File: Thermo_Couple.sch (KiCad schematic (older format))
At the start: 0 parts

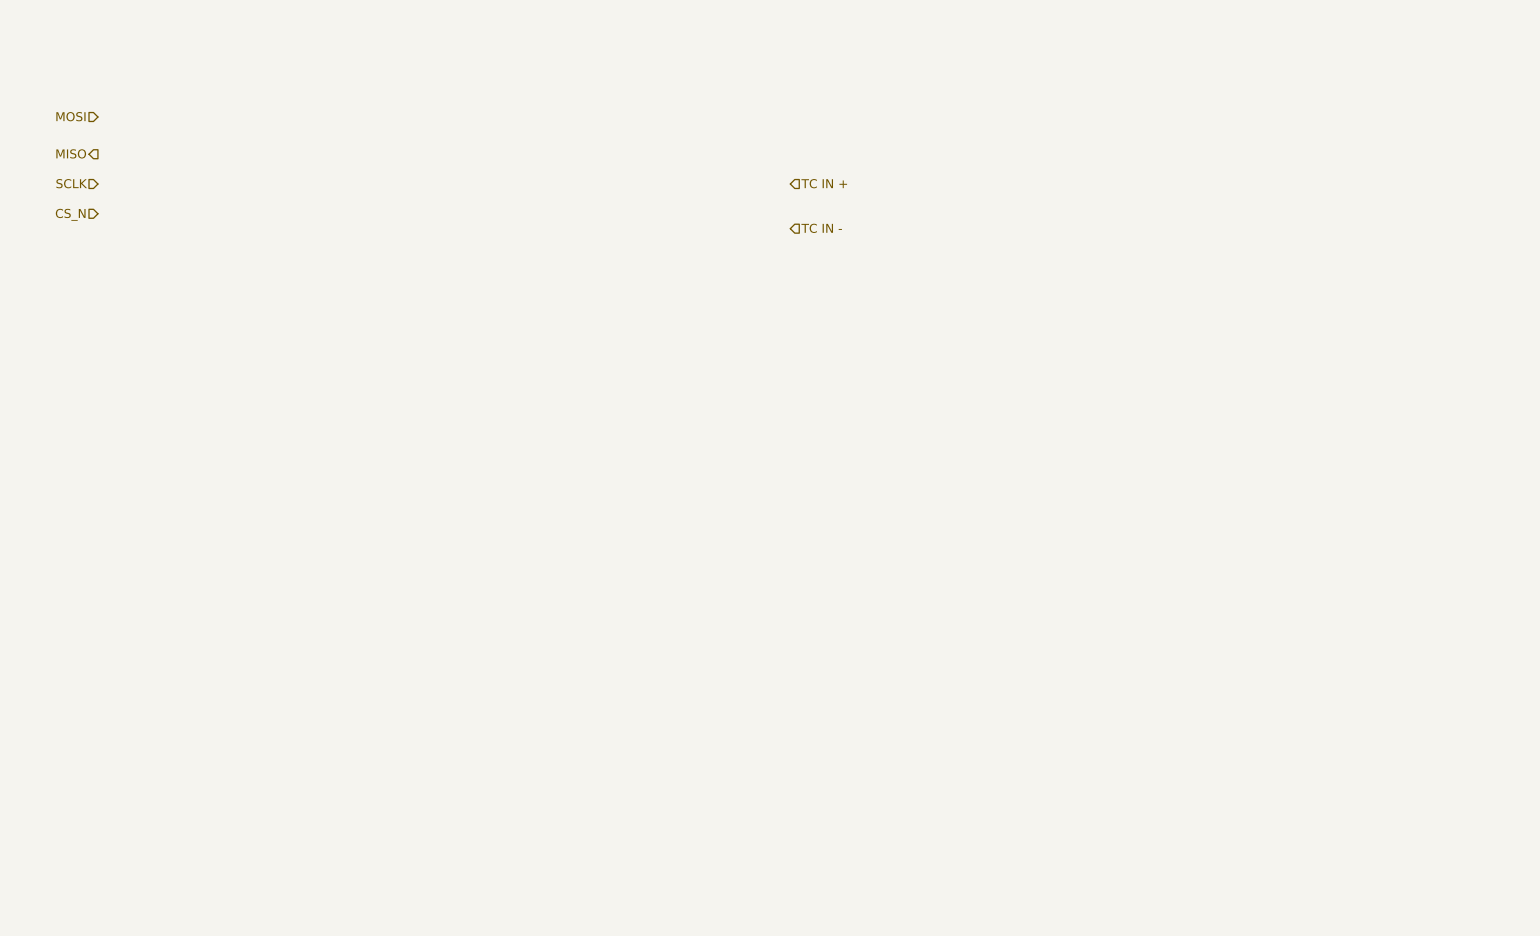
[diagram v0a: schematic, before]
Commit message: Wire Up general Thermocouple
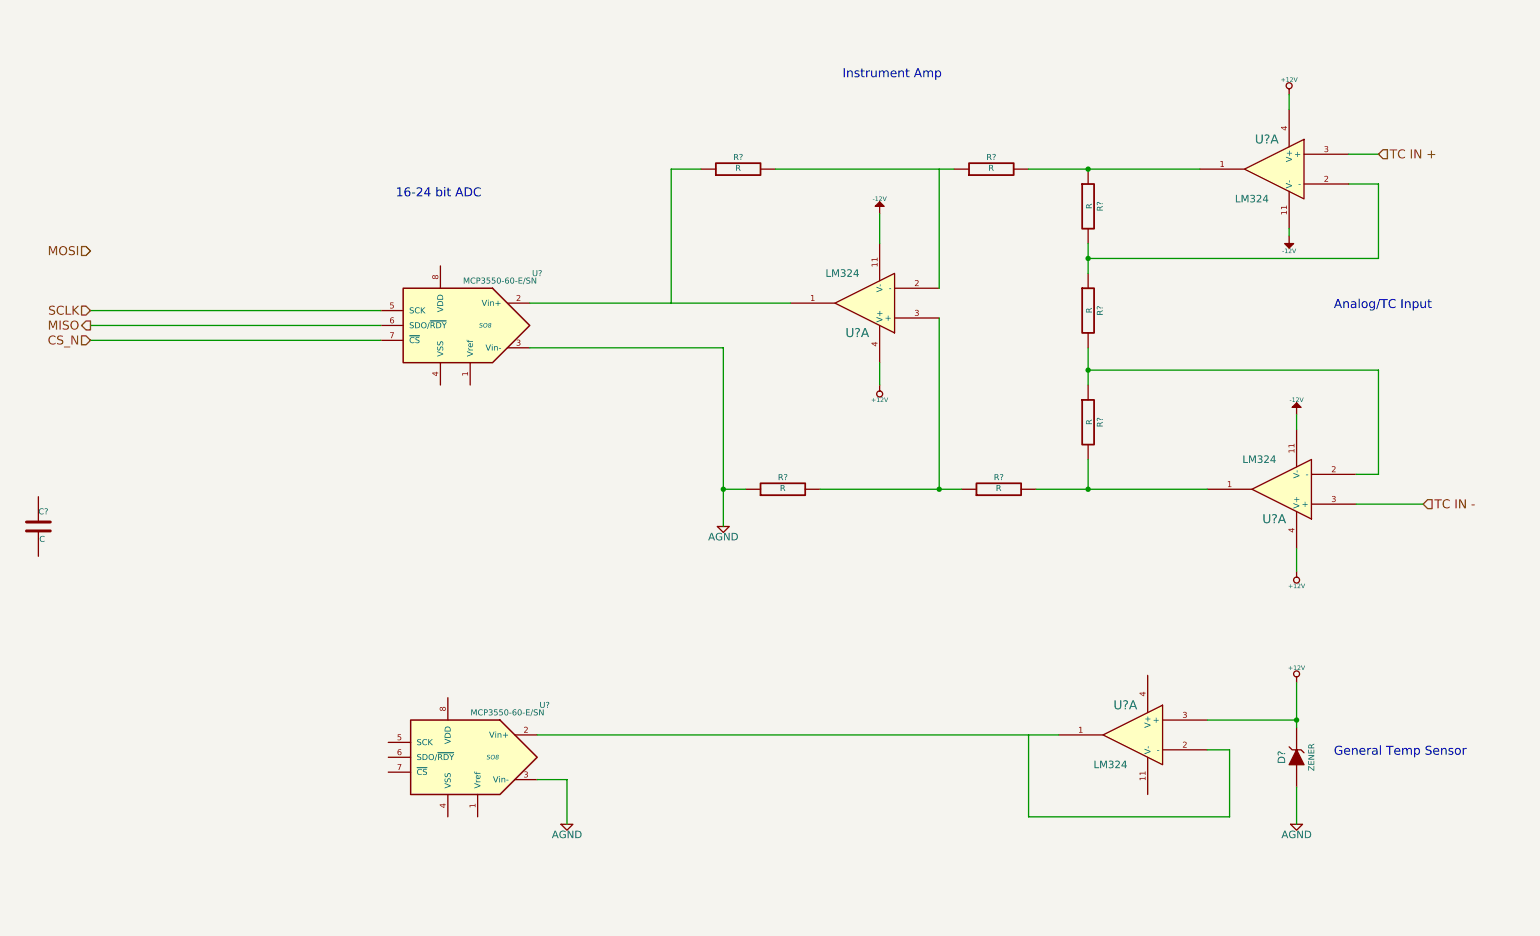
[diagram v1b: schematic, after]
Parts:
- added C?: C, ~, symbol C
- added D?: ZENER, ~, symbol ZENER
- added R? (x7): R, ~, symbol R
- added U? (x4): LM324, symbol LM324
- added U? (x2): MCP3550-60-E/SN, SO8, symbol MCP3550-60-E/SN
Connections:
- net labels added: +12V, -12V, AGND
- wire segments 0 -> 42
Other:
- note added: "16-24 bit ADC"
- note added: "Analog/TC Input"
- note added: "General Temp Sensor"
- note added: "Instrument Amp"

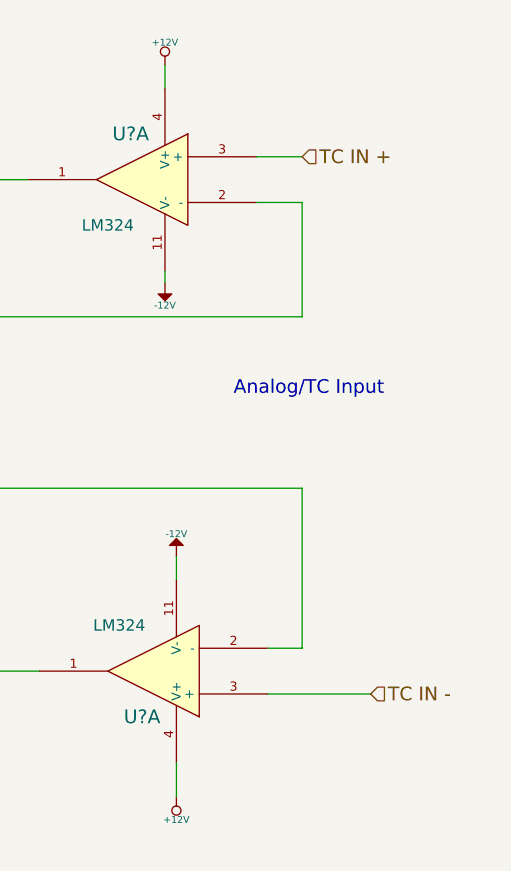
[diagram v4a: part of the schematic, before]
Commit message: Create Arduino Schematic and Wire Up top Level
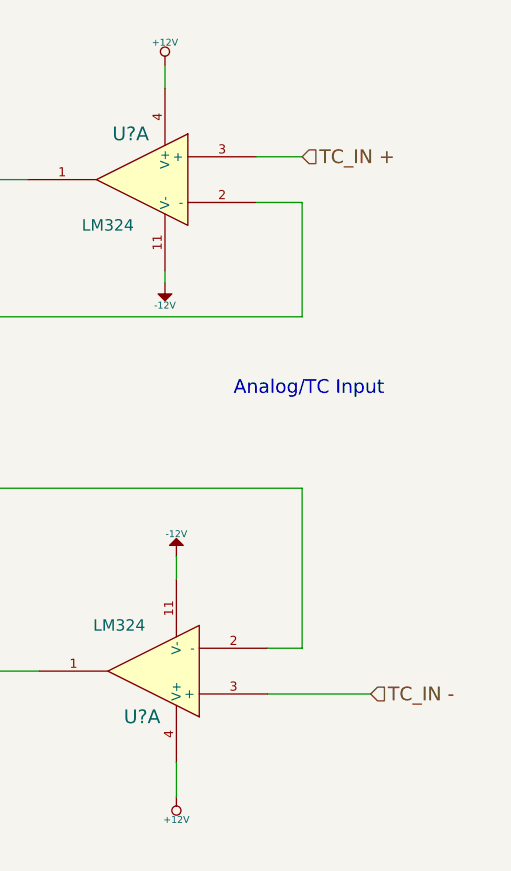
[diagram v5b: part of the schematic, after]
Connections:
- net labels added: TC_IN +, TC_IN -
- net labels removed: TC IN +, TC IN -
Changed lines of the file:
@@
 $EndDescr
 Text HLabel 10250 1800 2    60   Input ~ 0
-TC IN +
+TC_IN +
 Text HLabel 10550 4150 2    60   Input ~ 0
-TC IN -
+TC_IN -
 Text HLabel 1600 2950 0    60   Output ~ 0
 MISO

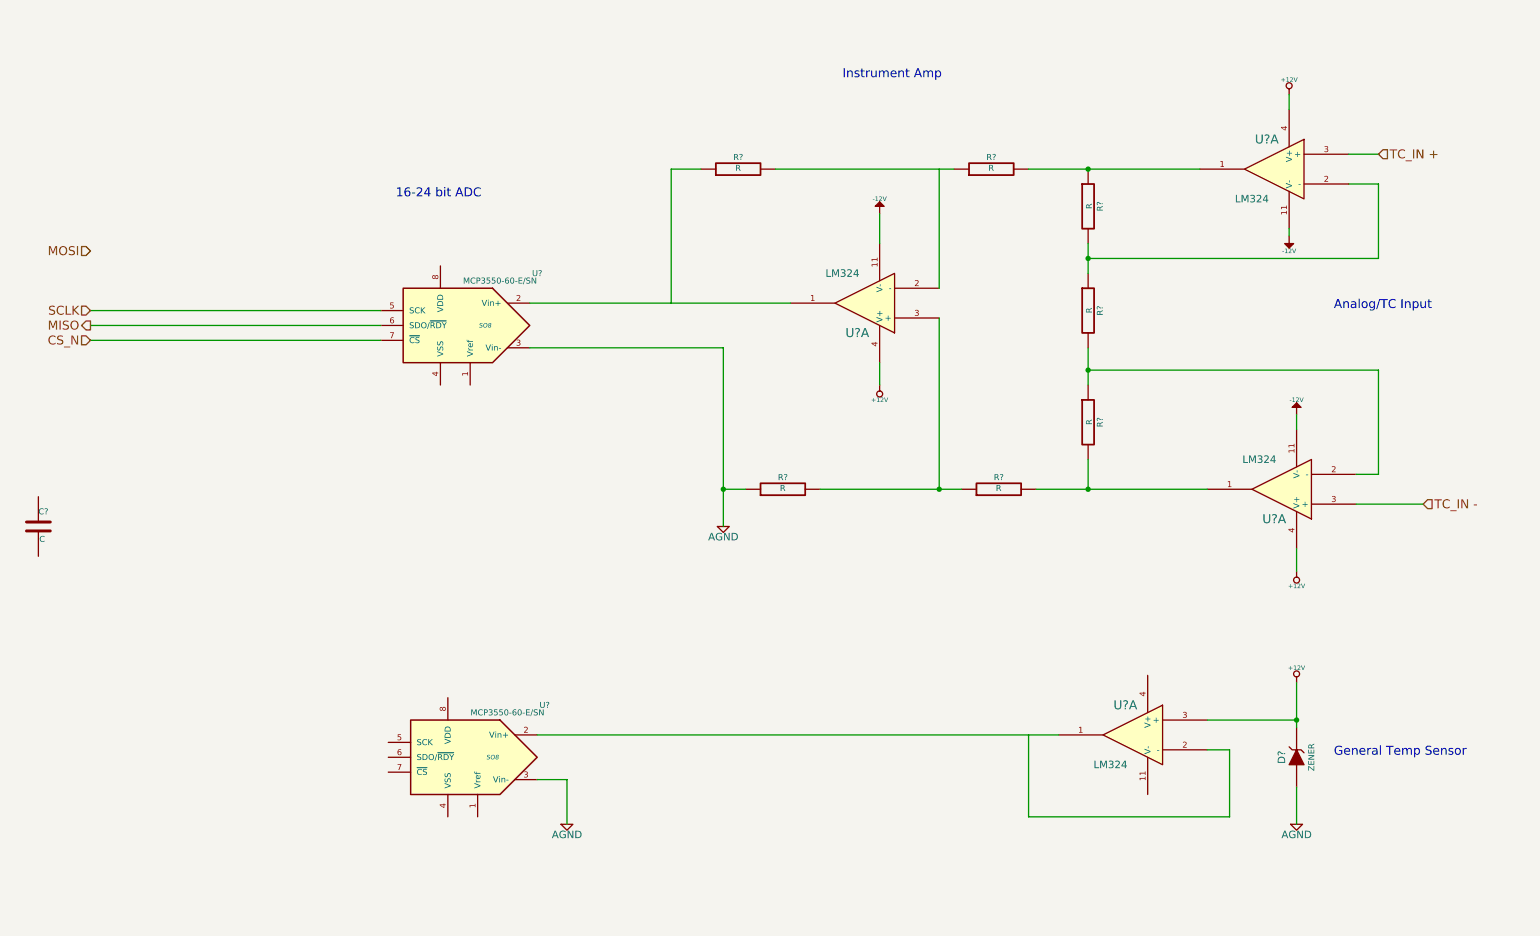
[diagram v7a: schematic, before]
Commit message: Added Arduino Connect Pin Layout
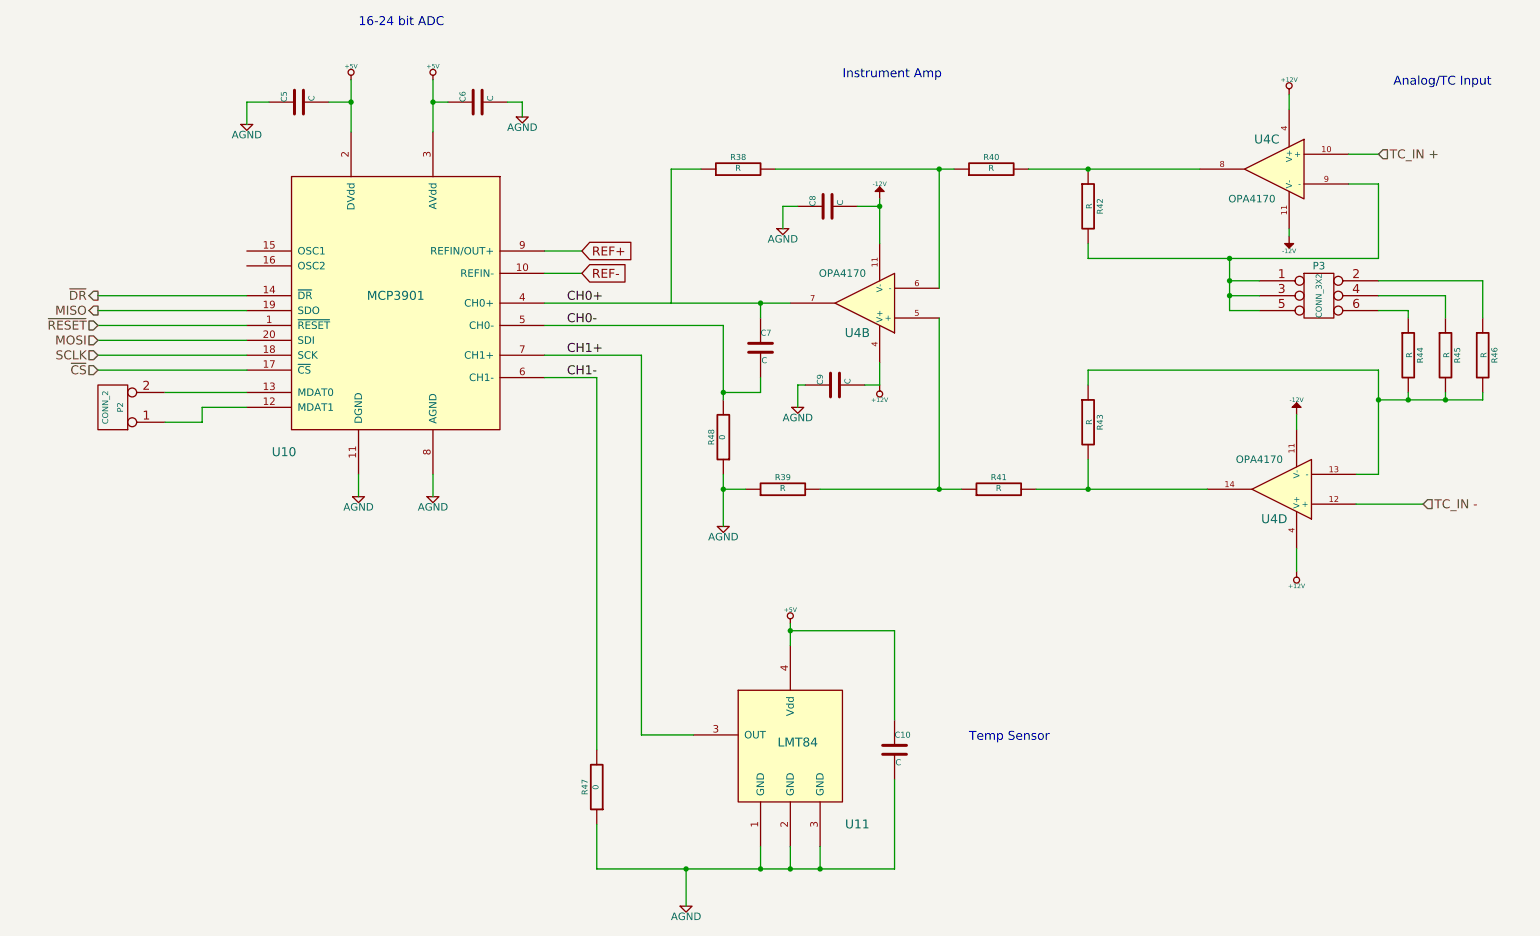
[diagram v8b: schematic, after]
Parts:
- removed C?: C, ~, symbol C
- removed D?: ZENER, ~, symbol ZENER
- removed U?: LM324, symbol LM324
- removed U? (x2): MCP3550-60-E/SN, SO8, symbol MCP3550-60-E/SN
- added C10, C5, C6, C7, C8, C9: C, ~, symbol C
- added P2: CONN_2, symbol CONN_2
- added P3: CONN_3X2, symbol CONN_3X2
- added R44, R45: R, ~, symbol R
- added R47, R48: 0, ~, symbol R
- added U10: MCP3901, symbol MCP3901
- added U11: LMT84, symbol LMT84
- U4: renamed from U?; value LM324 -> OPA4170
- gave numbers to parts that had none: 7
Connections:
- net labels added: +5V, CH0+, CH0-, CH1+, CH1-, REF+, REF-, ~CS, ~DR, ~RESET
- net labels removed: CS_N
- wire segments 42 -> 90
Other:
- note added: "Temp Sensor"
- note removed: "General Temp Sensor"
- moved on the sheet: R46
